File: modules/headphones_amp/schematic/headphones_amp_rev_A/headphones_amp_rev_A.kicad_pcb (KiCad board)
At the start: 2 copper layers, 120 x 100 mm, 110 parts, among them J1 AudioJack3_SwitchTR, J2 AudioJack3_SwitchTR, J3 Conn_01x02, J4 Conn_01x02, J5 Conn_01x02, J6 Conn_01x02, J7 Conn_01x02, Q1 BC140, Q10 BC548, Q11 BC548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

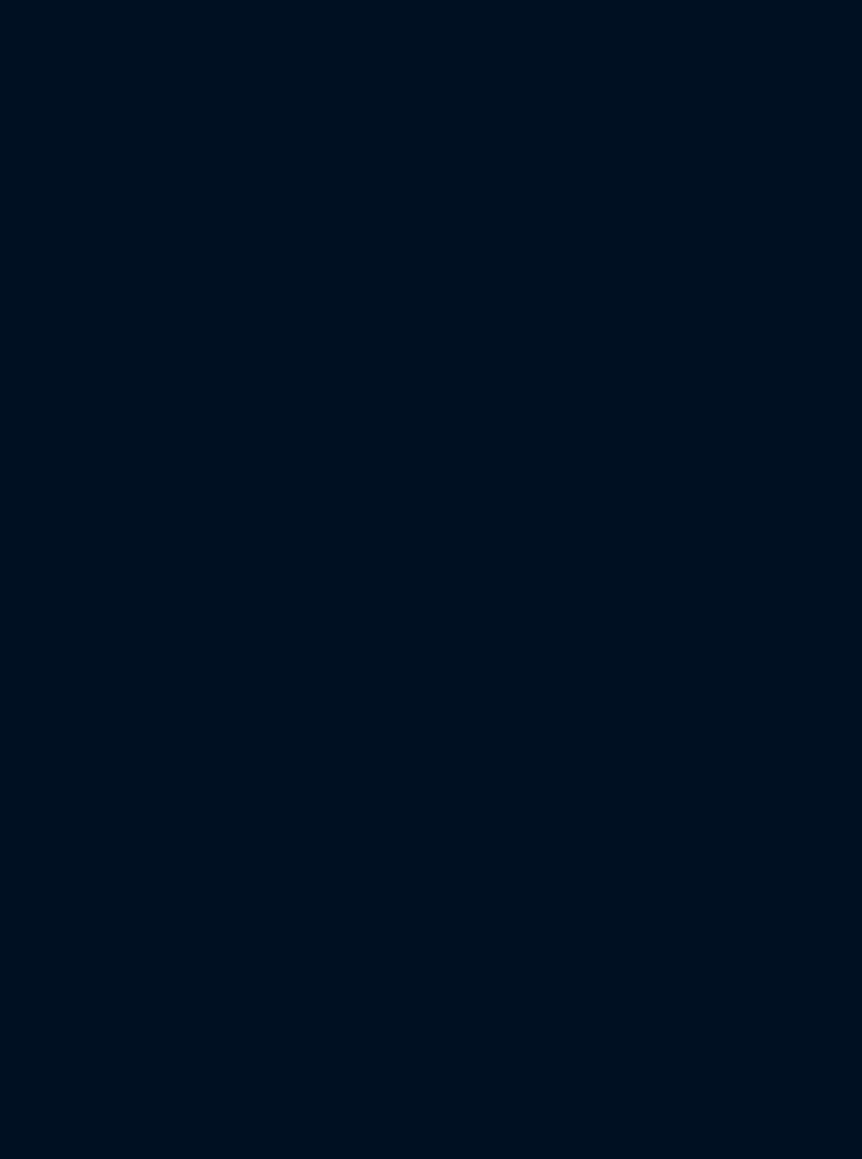
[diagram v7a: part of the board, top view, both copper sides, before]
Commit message: - added a bootstrap structure for improved input impedance - moved the mono/stereo junction point
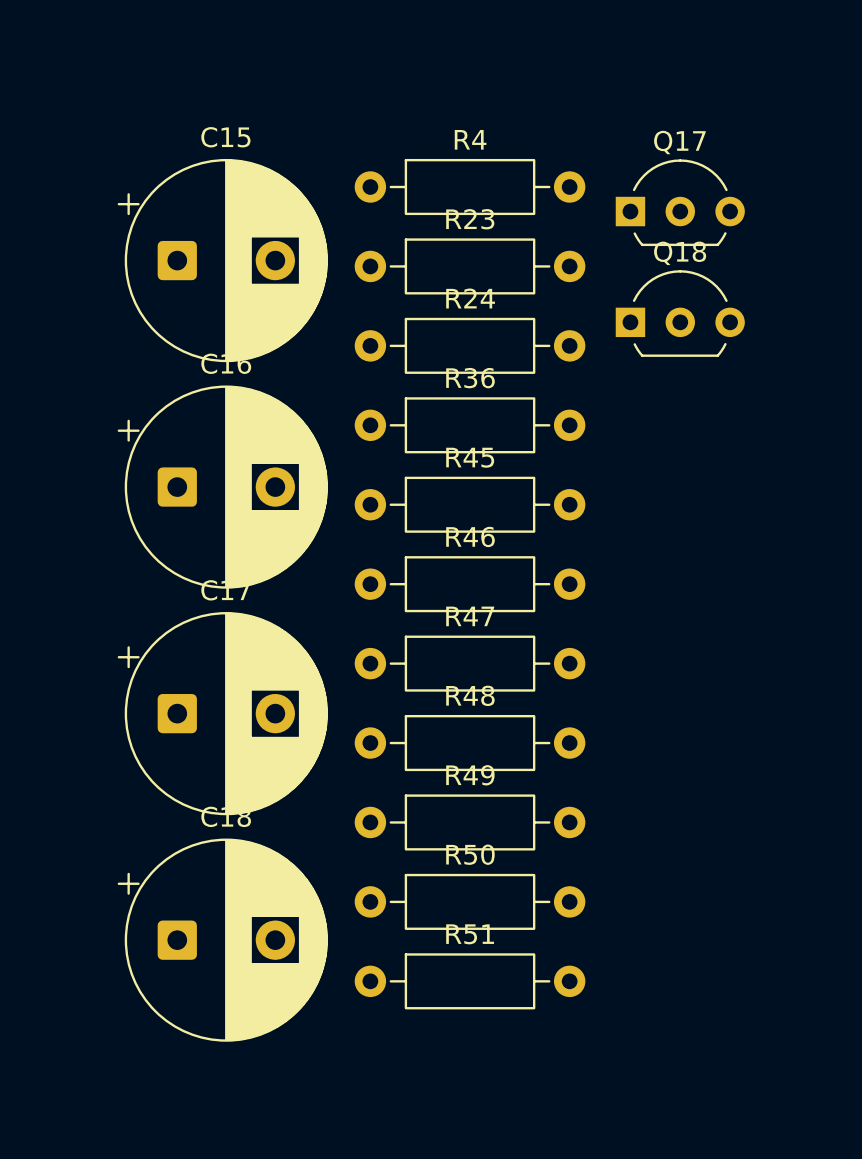
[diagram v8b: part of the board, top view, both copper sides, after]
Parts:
- added C15: 47µF, Capacitor_THT:CP_Radial_D10.0mm_P5.00mm, F.Cu at (180.0, 82.2)
- added C16: 220µ, Capacitor_THT:CP_Radial_D10.0mm_P5.00mm, F.Cu at (180.0, 93.8)
- added C17: 47µF, Capacitor_THT:CP_Radial_D10.0mm_P5.00mm, F.Cu at (180.0, 105.3)
- added C18: 220µ, Capacitor_THT:CP_Radial_D10.0mm_P5.00mm, F.Cu at (180.0, 116.9)
- added Q17: BC548, Package_TO_SOT_THT:TO-92L_Inline_Wide, F.Cu at (203.1, 79.8)
- added Q18: BC548, Package_TO_SOT_THT:TO-92L_Inline_Wide, F.Cu at (203.1, 85.4)
- added R23: 470, Resistor_THT:R_Axial_DIN0207_L6.3mm_D2.5mm_P10.16mm_Horizontal, F.Cu at (189.8, 82.5)
- added R24: 470, Resistor_THT:R_Axial_DIN0207_L6.3mm_D2.5mm_P10.16mm_Horizontal, F.Cu at (189.8, 86.6)
- added R36: 470, Resistor_THT:R_Axial_DIN0207_L6.3mm_D2.5mm_P10.16mm_Horizontal, F.Cu at (189.8, 90.7)
- added R4: 470, Resistor_THT:R_Axial_DIN0207_L6.3mm_D2.5mm_P10.16mm_Horizontal, F.Cu at (189.8, 78.5)
- added R45: 470, Resistor_THT:R_Axial_DIN0207_L6.3mm_D2.5mm_P10.16mm_Horizontal, F.Cu at (189.8, 94.7)
- added R46: 470, Resistor_THT:R_Axial_DIN0207_L6.3mm_D2.5mm_P10.16mm_Horizontal, F.Cu at (189.8, 98.8)
- added R47: 470, Resistor_THT:R_Axial_DIN0207_L6.3mm_D2.5mm_P10.16mm_Horizontal, F.Cu at (189.8, 102.8)
- added R48: 470, Resistor_THT:R_Axial_DIN0207_L6.3mm_D2.5mm_P10.16mm_Horizontal, F.Cu at (189.8, 106.8)
- added R49: 470, Resistor_THT:R_Axial_DIN0207_L6.3mm_D2.5mm_P10.16mm_Horizontal, F.Cu at (189.8, 110.9)
- added R50: 470, Resistor_THT:R_Axial_DIN0207_L6.3mm_D2.5mm_P10.16mm_Horizontal, F.Cu at (189.8, 115.0)
- added R51: 470, Resistor_THT:R_Axial_DIN0207_L6.3mm_D2.5mm_P10.16mm_Horizontal, F.Cu at (189.8, 119.0)
- RV3: value 68k -> 47k
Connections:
- C10 pad 1: Net-(C10-Pad1) -> Net-(Q18-B)
- C10 pad 2: Net-(Q9-B) -> Net-(RV3B-W)
- C9 pad 1: Net-(RV3A-W) -> Net-(Q17-B)
- C9 pad 2: Net-(Q8-B) -> Net-(RV3A-W)
- Q8 pad 2: Net-(Q8-B) -> Net-(Q17-C)
- Q9 pad 2: Net-(Q9-B) -> Net-(Q18-C)
- R22 pad 2: Net-(Q8-B) -> Net-(Q17-C)
- SW2 pad 1: Net-(RV3A-W) -> unconnected-(SW2-Pad1)
- SW2 pad 2: Net-(C10-Pad1) -> unconnected-(SW2-Pad2)
- SW2 pad 3: Net-(RV3B-W) -> unconnected-(SW2-Pad3)
